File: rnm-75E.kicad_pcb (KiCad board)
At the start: 2 copper layers, 323.8 x 114.3 mm, 217 parts, among them J1 AVR-ISP-6, J2 USB_C_Receptacle_USB2.0, J3 Conn_01x04, SW1 SW_Push, SW2 Rotary_Encoder_Switch, U1 AT90USB646-AU, Y1 Crystal_GND24_Small

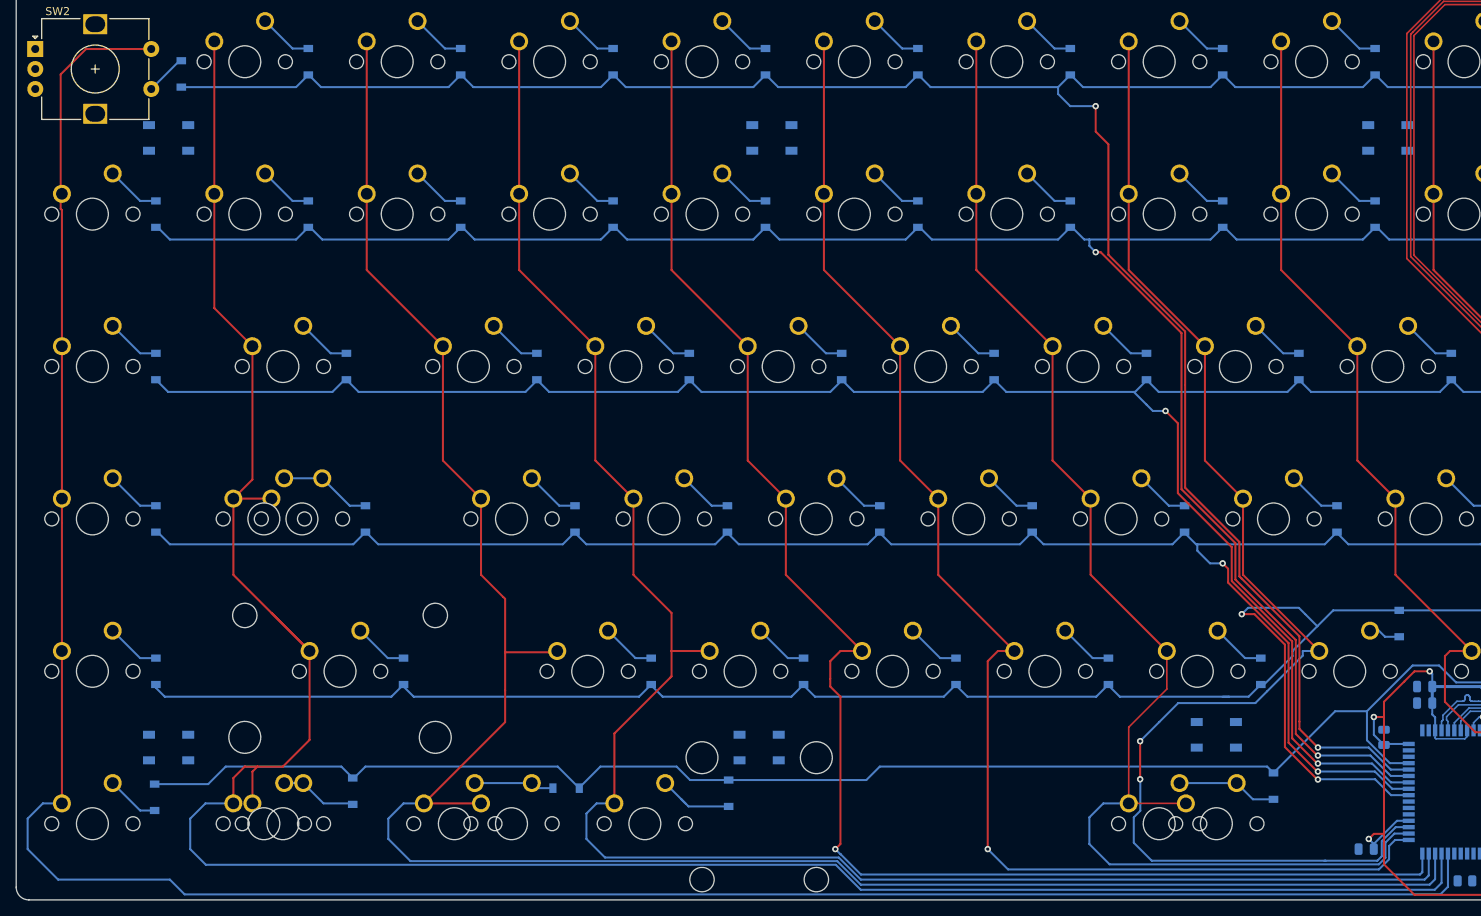
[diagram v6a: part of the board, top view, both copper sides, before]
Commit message: routed encoder
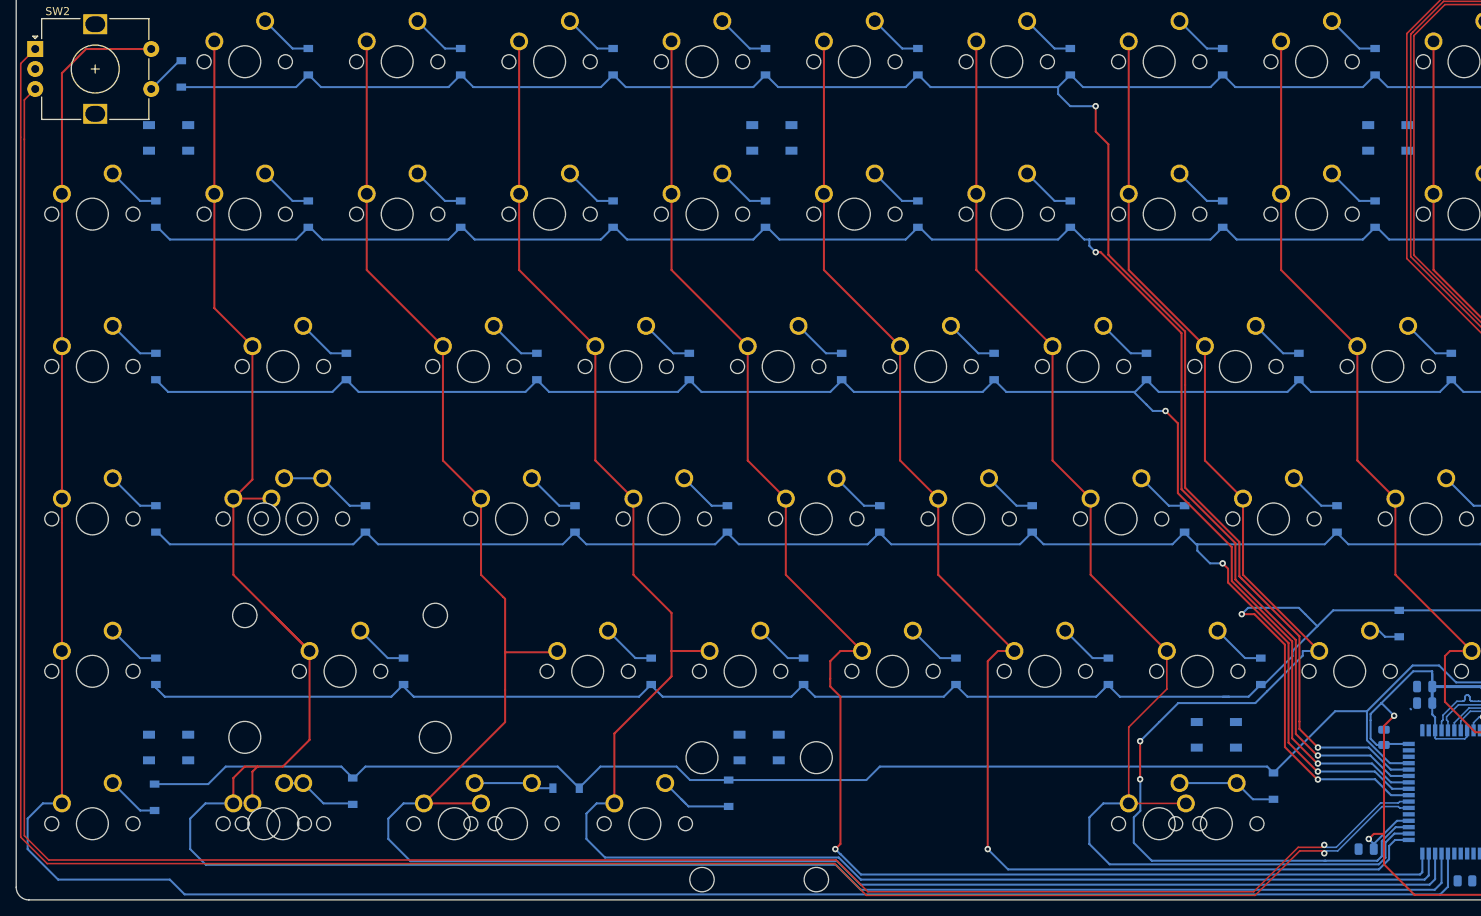
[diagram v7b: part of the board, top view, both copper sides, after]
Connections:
- F1 pad 2: ENCODER_A -> ENCODER+
- J1 pad 2: ENCODER_A -> ENCODER+
- J2 pad A4: ENCODER_A -> ENCODER+
- J2 pad A9: ENCODER_A -> ENCODER+
- J2 pad B4: ENCODER_A -> ENCODER+
- J2 pad B9: ENCODER_A -> ENCODER+
- SW2 pad A: ENCODER_A -> ENCODER+
- SW2 pad B: ENCODER_A -> ENCODER+
- U1 pad 1: ENCODER_A -> (no net)
- U1 pad 2: ENCODER_A -> (no net)
- U1 pad 54: (no net) -> ENCODER+
- U1 pad 55: (no net) -> ENCODER+
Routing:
- net ENCODER+: track 0.00 -> 560.1 mm, vias 0 -> 2
- net COL0: track 297.1 -> 314.0 mm
- net +5V: track 345.4 -> 350.3 mm, vias 6 -> 5
- net ENCODER_A: track 4.52 -> 0.11 mm
- net (no net): track 0.00 -> 0.68 mm

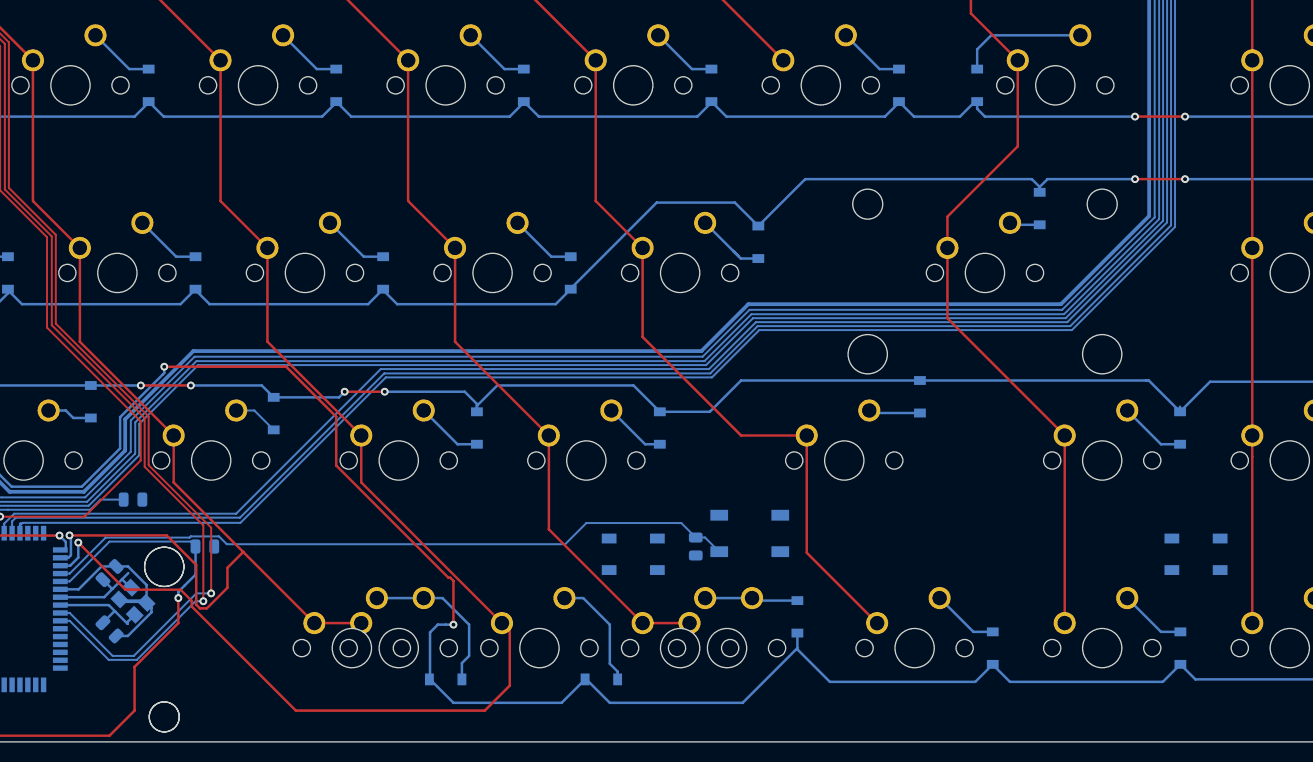
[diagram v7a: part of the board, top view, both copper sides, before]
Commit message: Route rows 11/-15
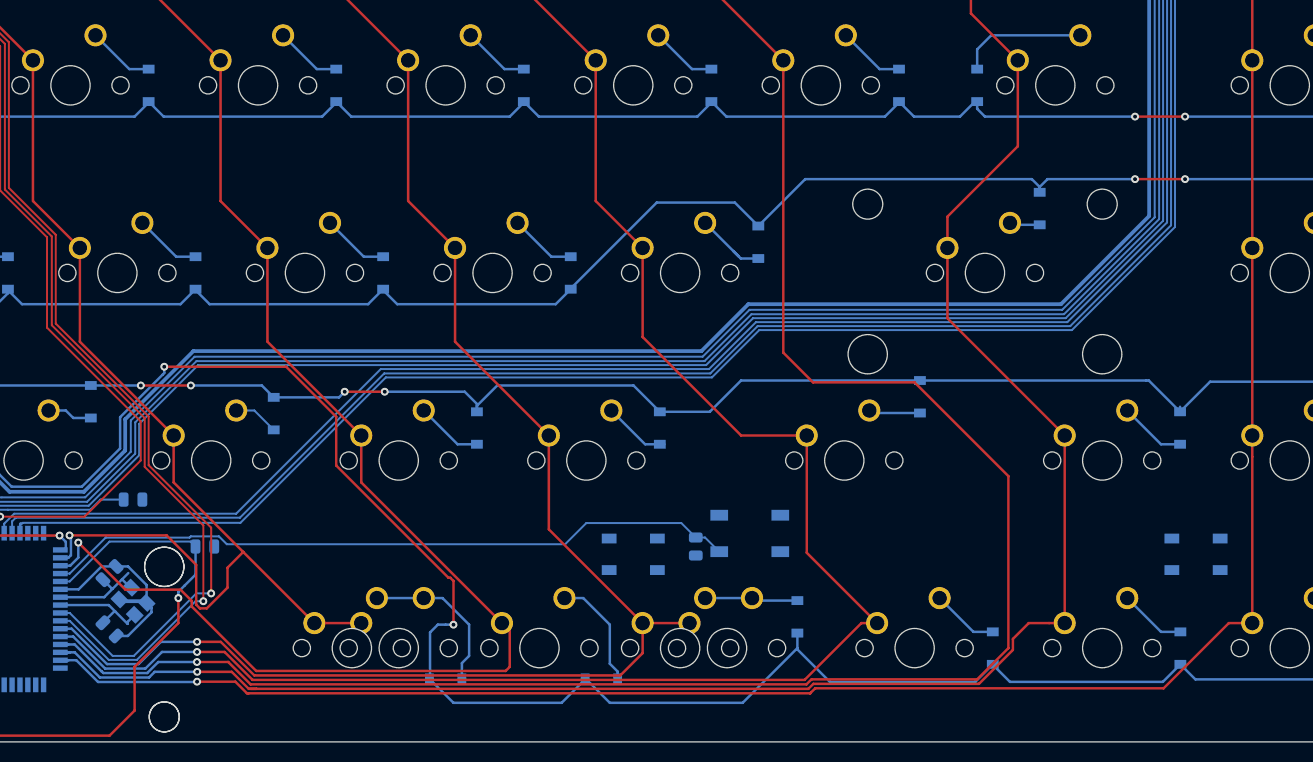
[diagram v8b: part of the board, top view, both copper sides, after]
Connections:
- U1 pad 27: (no net) -> COL11
- U1 pad 28: COL15 -> COL12
- U1 pad 29: COL14 -> COL13
- U1 pad 30: COL13 -> COL14
- U1 pad 31: COL12 -> COL15
- U1 pad 32: COL11 -> (no net)
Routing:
- net COL13: track 42.0 -> 218.5 mm, vias 0 -> 1
- net COL15: track 76.2 -> 202.5 mm, vias 0 -> 1
- net COL14: track 109.1 -> 218.0 mm, vias 0 -> 1
- net COL12: track 114.9 -> 203.5 mm, vias 0 -> 1
- net COL11: track 113.8 -> 180.8 mm, vias 0 -> 1
- net COL10: track 173.7 -> 169.2 mm
